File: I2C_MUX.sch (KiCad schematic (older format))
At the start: 25 parts, among them U5 TCA9548ARGER

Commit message: pcb progress
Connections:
- net labels removed: I2C_SFP3_SCL, I2C_SFP3_SDA, I2C_SFP4_SCL, I2C_SFP4_SDA
- wire segments 94 -> 90
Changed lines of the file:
@@
 Text HLabel 7850 3200 2    50   Output ~ 10
 I2C_SFP2_SCL
-Text HLabel 7850 3100 2    50   BiDi ~ 10
-I2C_SFP3_SDA
-Text HLabel 7850 3000 2    50   Output ~ 10
-I2C_SFP3_SCL
-Text HLabel 7850 2900 2    50   BiDi ~ 10
-I2C_SFP4_SDA
-Text HLabel 7850 2800 2    50   Output ~ 10
-I2C_SFP4_SCL
 Text HLabel 7850 2200 2    50   Output ~ 10
 I2C_FMC1_SCL
@@
 Text Label 7000 3300 0    50   ~ 10
 I2C_SFP2_SDA
-Text Label 7000 3000 0    50   ~ 10
-I2C_SFP3_SCL
-Text Label 7000 3100 0    50   ~ 10
-I2C_SFP3_SDA
-Text Label 7000 2800 0    50   ~ 10
-I2C_SFP4_SCL
-Text Label 7000 2900 0    50   ~ 10
-I2C_SFP4_SDA
 Text Label 7000 3400 0    50   ~ 10
 I2C_APP_SCL
@@
 	6000 3300 7850 3300
 Wire Wire Line
-	6000 3000 7850 3000
-Connection ~ 6000 3000
-Wire Wire Line
-	6000 3100 7850 3100
-Connection ~ 6000 3100
-Wire Wire Line
-	6000 2800 7850 2800
-Wire Wire Line
-	6000 2900 7850 2900
-Wire Wire Line
 	6000 3400 7850 3400
 Connection ~ 6000 3400
@@
 	6000 3700 7850 3700
 Connection ~ 6000 3700
-Connection ~ 6000 2800
-Connection ~ 6000 2900
 Connection ~ 6000 3200
 Connection ~ 6000 3300

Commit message: FPGA power finished, significant progress on PCB
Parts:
- U5: symbol AMC_FMC_Carrier-PcbDoc-rescue:TCA9548ARGER-Interface_Expansion-AMC_FMC_Carrier-PcbDoc-rescue -> AMC_FMC_Carrier-PcbDoc-rescue:TCA9548ARGER-Interface_Expansion-AMC_FMC_Carrier-PcbDoc-rescue-AMC_FMC_Carrier-PcbDoc-res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
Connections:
- net labels added: QSFP_SCL, QSFP_SDA
- net labels removed: I2C_SFP2_SCL, I2C_SFP2_SDA
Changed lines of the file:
@@
 $EndDescr
 $Comp
-L AMC_FMC_Carrier-PcbDoc-rescue:TCA9548ARGER-Interface_Expansion-AMC_FMC_Carrier-PcbDoc-rescue U5
+L AMC_FMC_Carrier-PcbDoc-rescue:TCA9548ARGER-Interface_Expansion-AMC_FMC_Carrier-PcbDoc-rescue-AMC_FMC_Carrier-PcbDoc-rescue-AMC_FMC_Carrier-PcbDoc-rescue U5
 U 1 1 5C5DB690
 P 5150 2900
@@
 I2C_SFP1_SCL
 Text HLabel 7850 3300 2    50   BiDi ~ 10
-I2C_SFP2_SDA
+QSFP_SDA
 Text HLabel 7850 3200 2    50   Output ~ 10
-I2C_SFP2_SCL
+QSFP_SCL
 Text HLabel 7850 2200 2    50   Output ~ 10
 I2C_FMC1_SCL
@@
 I2C_SFP1_SDA
 Text Label 7000 3200 0    50   ~ 10
-I2C_SFP2_SCL
+QSFP_SCL
 Text Label 7000 3300 0    50   ~ 10
-I2C_SFP2_SDA
+QSFP_SDA
 Text Label 7000 3400 0    50   ~ 10
 I2C_APP_SCL

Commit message: new board outline, rearranging banks connections, SODIMM memory
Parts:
- U5: symbol AMC_FMC_Carrier-PcbDoc-rescue:TCA9548ARGER-Interface_Expansion-AMC_FMC_Carrier-PcbDoc-rescue-AMC_FMC_Carrier-PcbDoc-rescue-AMC_FMC_Carrier-PcbDoc-rescue -> AMC_FMC_Carrier-PcbDoc-rescue:TCA9548ARGER-Interface_Expansion-AMC_FMC_Carrier-PcbDoc-rescue-AMC_FMC_Carrier-PcbDoc-rescue
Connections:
- net +3V3: no longer C40.2, R274.1, R39.1, R40.1, R41.1, U5.21 (VCC)
- net QSFP1_SCL: now reaches R53.1, U5.11 (SC4)
- net QSFP1_SDA: now reaches R54.1, U5.10 (SD4)
- net I2C_SFP1_SCL renamed I2C_CLK_SCL
- net I2C_SFP1_SDA renamed I2C_CLK_SDA
- net QSFP_SCL renamed QSFP2_SCL
- net QSFP_SDA renamed QSFP2_SDA
- new net +3.3VP: C40.2, R274.1, R39.1, R40.1, R41.1, U5.21 (VCC)
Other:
- note removed: "FMC1\n\n"
- note removed: "FMC2\n\n"
- note removed: "SFP1\n"
- note removed: "SFP2\n\n"
- note removed: "SFP3\n\n"
- note removed: "SFP4\n"
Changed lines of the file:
@@
 EESchema Schematic File Version 4
-LIBS:AMC_FMC_Carrier-PcbDoc-cache
 EELAYER 30 0
 EELAYER END
 $Descr A4 11693 8268
 encoding utf-8
-Sheet 7 25
+Sheet 5 25
 Title "Marble"
 Date "2019-01-16"
@@
 $EndDescr
 $Comp
-L AMC_FMC_Carrier-PcbDoc-rescue:TCA9548ARGER-Interface_Expansion-AMC_FMC_Carrier-PcbDoc-rescue-AMC_FMC_Carrier-PcbDoc-rescue-AMC_FMC_Carrier-PcbDoc-rescue U5
+L AMC_FMC_Carrier-PcbDoc-rescue:TCA9548ARGER-Interface_Expansion-AMC_FMC_Carrier-PcbDoc-rescue-AMC_FMC_Carrier-PcbDoc-rescue U5
 U 1 1 5C5DB690
 P 5150 2900
@@
 	1    0    0    -1
 $EndComp
-Text Notes 6600 2250 0    50   ~ 10
-FMC1\n\n
-Text Notes 6600 2450 0    50   ~ 10
-FMC2\n\n
-Text Notes 6600 2600 0    50   ~ 10
-SFP1\n
-Text Notes 6600 3250 0    50   ~ 10
-SFP2\n\n
-Text Notes 6600 3050 0    50   ~ 10
-SFP3\n\n
-Text Notes 6600 2800 0    50   ~ 10
-SFP4\n
-$Comp
-L power:+3V3 #PWR?
-U 1 1 5C5F9FA2
-P 5150 1700
-AR Path="/5BD32060/5C5F9FA2" Ref="#PWR?"  Part="1"
-AR Path="/5BABAC65/5C5F9FA2" Ref="#PWR?"  Part="1"
-AR Path="/5CC24E97/5C5F9FA2" Ref="#PWR?"  Part="1"
-AR Path="/5CC393D3/5C5F9FA2" Ref="#PWR?"  Part="1"
-AR Path="/5CC6DBF7/5C5F9FA2" Ref="#PWR?"  Part="1"
-AR Path="/5CC8AFE1/5C5F9FA2" Ref="#PWR?"  Part="1"
-AR Path="/5BCEDA3D/5C5F9FA2" Ref="#PWR065"  Part="1"
-F 0 "#PWR065" H 5150 1550 50  0001 C CNN
-F 1 "+3V3" H 5165 1873 50  0000 C CNN
-F 2 "" H 5150 1700 50  0001 C CNN
-F 3 "" H 5150 1700 50  0001 C CNN
-	1    5150 1700
-	1    0    0    -1
-$EndComp
 Wire Wire Line
 	5150 1700 5150 1800
@@
 Wire Wire Line
 	4600 3400 4750 3400
-Text HLabel 7850 2700 2    50   BiDi ~ 10
-I2C_SFP1_SDA
-Text HLabel 7850 2600 2    50   Output ~ 10
-I2C_SFP1_SCL
 Text HLabel 7850 3300 2    50   BiDi ~ 10
-QSFP_SDA
+QSFP2_SDA
 Text HLabel 7850 3200 2    50   Output ~ 10
-QSFP_SCL
+QSFP2_SCL
 Text HLabel 7850 2200 2    50   Output ~ 10
 I2C_FMC1_SCL
@@
 	6000 2450 6000 2500
 Wire Wire Line
-	6000 2550 6000 2600
-Wire Wire Line
-	6000 2650 6000 2700
-Wire Wire Line
 	6000 2750 6000 2800
 Wire Wire Line
 	6000 2850 6000 2900
 Wire Wire Line
-	6000 2950 6000 3000
-Wire Wire Line
-	6000 3050 6000 3100
-Wire Wire Line
 	6000 3150 6000 3200
 Wire Wire Line
@@
 	5550 2600 6000 2600
 Wire Wire Line
-	5550 2700 6000 2700
-Wire Wire Line
 	5550 2800 6000 2800
 Wire Wire Line
@@
 	1    0    0    -1
 $EndComp
-$Comp
-L power:+3V3 #PWR?
-U 1 1 5C2D28CD
-P 4050 1700
-AR Path="/5BD32060/5C2D28CD" Ref="#PWR?"  Part="1"
-AR Path="/5BABAC65/5C2D28CD" Ref="#PWR?"  Part="1"
-AR Path="/5CC24E97/5C2D28CD" Ref="#PWR?"  Part="1"
-AR Path="/5CC393D3/5C2D28CD" Ref="#PWR?"  Part="1"
-AR Path="/5CC6DBF7/5C2D28CD" Ref="#PWR?"  Part="1"
-AR Path="/5CC8AFE1/5C2D28CD" Ref="#PWR?"  Part="1"
-AR Path="/5BCEDA3D/5C2D28CD" Ref="#PWR062"  Part="1"
-F 0 "#PWR062" H 4050 1550 50  0001 C CNN
-F 1 "+3V3" H 4065 1873 50  0000 C CNN
-F 2 "" H 4050 1700 50  0001 C CNN
-F 3 "" H 4050 1700 50  0001 C CNN
-	1    4050 1700
-	1    0    0    -1
-$EndComp
 Wire Wire Line
 	4250 1750 4250 1700
@@
 Wire Wire Line
 	4050 1750 4050 1700
-Connection ~ 4050 1700
 Wire Wire Line
 	4050 2050 4050 2200
@@
 Text Label 7000 2500 0    50   ~ 10
 I2C_FMC2_SDA
-Text Label 7000 2600 0    50   ~ 10
-I2C_SFP1_SCL
-Text Label 7000 2700 0    50   ~ 10
-I2C_SFP1_SDA
 Text Label 7000 3200 0    50   ~ 10
-QSFP_SCL
+QSFP2_SCL
 Text Label 7000 3300 0    50   ~ 10
-QSFP_SDA
+QSFP2_SDA
 Text Label 7000 3400 0    50   ~ 10
 I2C_APP_SCL
@@
 Connection ~ 6000 2500
 Wire Wire Line
-	6000 2600 7850 2600
-Connection ~ 6000 2600
-Wire Wire Line
-	6000 2700 7850 2700
-Connection ~ 6000 2700
-Wire Wire Line
 	6000 3200 7850 3200
 Wire Wire Line
@@
 	0    1    1    0
 $EndComp
-$Comp
-L power:+3V3 #PWR?
-U 1 1 5D00ED85
-P 4450 2850
-AR Path="/5BD32060/5D00ED85" Ref="#PWR?"  Part="1"
-AR Path="/5BABAC65/5D00ED85" Ref="#PWR?"  Part="1"
-AR Path="/5CC24E97/5D00ED85" Ref="#PWR?"  Part="1"
-AR Path="/5CC393D3/5D00ED85" Ref="#PWR?"  Part="1"
-AR Path="/5CC6DBF7/5D00ED85" Ref="#PWR?"  Part="1"
-AR Path="/5CC8AFE1/5D00ED85" Ref="#PWR?"  Part="1"
-AR Path="/5BCEDA3D/5D00ED85" Ref="#PWR0648"  Part="1"
-F 0 "#PWR0648" H 4450 2700 50  0001 C CNN
-F 1 "+3V3" V 4450 3050 50  0000 C CNN
-F 2 "" H 4450 2850 50  0001 C CNN
-F 3 "" H 4450 2850 50  0001 C CNN
-	1    4450 2850
-	0    -1   -1   0
-$EndComp
 Wire Wire Line
 	4450 2850 4650 2850
@@
 Text Notes 2600 7300 0    79   ~ 16
 8 bit I2C addresses ( R/W bit = 0)
+Text HLabel 7850 3100 2    50   BiDi ~ 10
+QSFP1_SDA
+Text HLabel 7850 3000 2    50   Output ~ 10
+QSFP1_SCL
+Text Label 7000 3000 0    50   ~ 10
+QSFP1_SCL
+Text Label 7000 3100 0    50   ~ 10
+QSFP1_SDA
+Wire Wire Line
+	6000 3000 7850 3000
+Wire Wire Line
+	6000 3100 7850 3100
+Wire Wire Line
+	6000 2950 6000 3000
+Connection ~ 6000 3000
+Wire Wire Line
+	6000 3050 6000 3100
+Connection ~ 6000 3100
+Text HLabel 7850 2600 2    50   Output ~ 10
+I2C_CLK_SCL
+Text HLabel 7850 2700 2    50   BiDi ~ 10
+I2C_CLK_SDA
+Text Label 7000 2600 0    50   ~ 10
+I2C_CLK_SCL
+Text Label 7000 2700 0    50   ~ 10
+I2C_CLK_SDA
+Wire Wire Line
+	6000 2600 7850 2600
+Wire Wire Line
+	6000 2550 6000 2600
+Wire Wire Line
+	5550 2700 6000 2700
+Connection ~ 6000 2600
+Wire Wire Line
+	6000 2650 6000 2700
+Connection ~ 6000 2700
+Wire Wire Line
+	6000 2700 7850 2700
+$Comp
+L power:+3.3VP #PWR?
+U 1 1 5F60B33D
+P 5150 1700
+AR Path="/5C16C03C/5F60B33D" Ref="#PWR?"  Part="1"
+AR Path="/5BCEDA39/5F60B33D" Ref="#PWR?"  Part="1"
+AR Path="/5D05A99E/5F60B33D" Ref="#PWR?"  Part="1"
+AR Path="/5C16BF8E/5F60B33D" Ref="#PWR?"  Part="1"
+AR Path="/5F60B33D" Ref="#PWR?"  Part="1"
+AR Path="/5BCEDA3D/5F60B33D" Ref="#PWR?"  Part="1"
+F 0 "#PWR?" H 5150 1550 50  0001 C CNN
+F 1 "+3V3MP" H 5165 1873 50  0000 C CNN
+F 2 "" H 5150 1700 50  0001 C CNN
+F 3 "" H 5150 1700 50  0001 C CNN
+	1    5150 1700
+	1    0    0    -1
+$EndComp
+$Comp
+L power:+3.3VP #PWR?
+U 1 1 5F60D5A3
+P 4050 1700
+AR Path="/5C16C03C/5F60D5A3" Ref="#PWR?"  Part="1"
+AR Path="/5BCEDA39/5F60D5A3" Ref="#PWR?"  Part="1"
+AR Path="/5D05A99E/5F60D5A3" Ref="#PWR?"  Part="1"
+AR Path="/5C16BF8E/5F60D5A3" Ref="#PWR?"  Part="1"
+AR Path="/5F60D5A3" Ref="#PWR?"  Part="1"
+AR Path="/5BCEDA3D/5F60D5A3" Ref="#PWR?"  Part="1"
+F 0 "#PWR?" H 4050 1550 50  0001 C CNN
+F 1 "+3V3MP" H 4065 1873 50  0000 C CNN
+F 2 "" H 4050 1700 50  0001 C CNN
+F 3 "" H 4050 1700 50  0001 C CNN
+	1    4050 1700
+	1    0    0    -1
+$EndComp
+$Comp
+L power:+3.3VP #PWR?
+U 1 1 5F60F78D
+P 4450 2850
+AR Path="/5C16C03C/5F60F78D" Ref="#PWR?"  Part="1"
+AR Path="/5BCEDA39/5F60F78D" Ref="#PWR?"  Part="1"
+AR Path="/5D05A99E/5F60F78D" Ref="#PWR?"  Part="1"
+AR Path="/5C16BF8E/5F60F78D" Ref="#PWR?"  Part="1"
+AR Path="/5F60F78D" Ref="#PWR?"  Part="1"
+AR Path="/5BCEDA3D/5F60F78D" Ref="#PWR?"  Part="1"
+F 0 "#PWR?" H 4450 2700 50  0001 C CNN
+F 1 "+3V3MP" V 4450 3100 50  0000 C CNN
+F 2 "" H 4450 2850 50  0001 C CNN
+F 3 "" H 4450 2850 50  0001 C CNN
+	1    4450 2850
+	0    -1   -1   0
+$EndComp
+Connection ~ 4050 1700
 $EndSCHEMATC

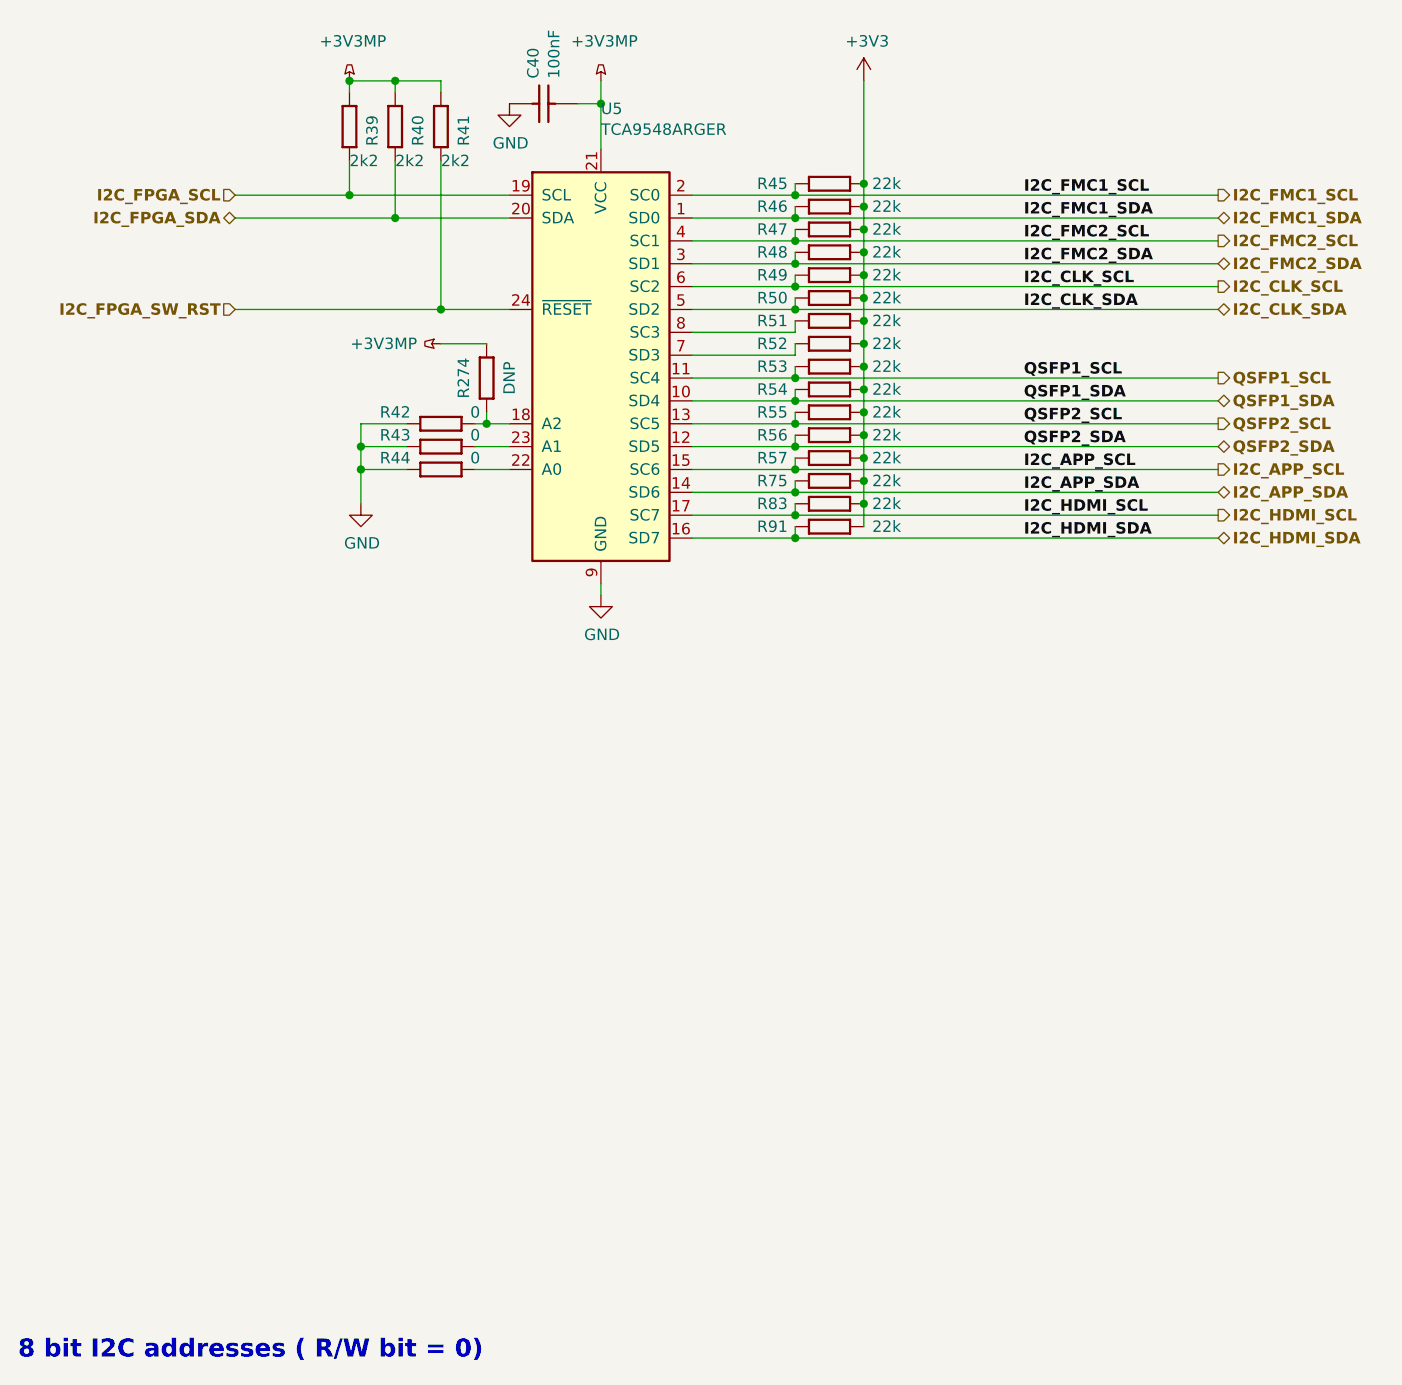
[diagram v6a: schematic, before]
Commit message: DDR lenght mached, 2 additional LEDs added, I2C pullups voltage changed and other minor changes
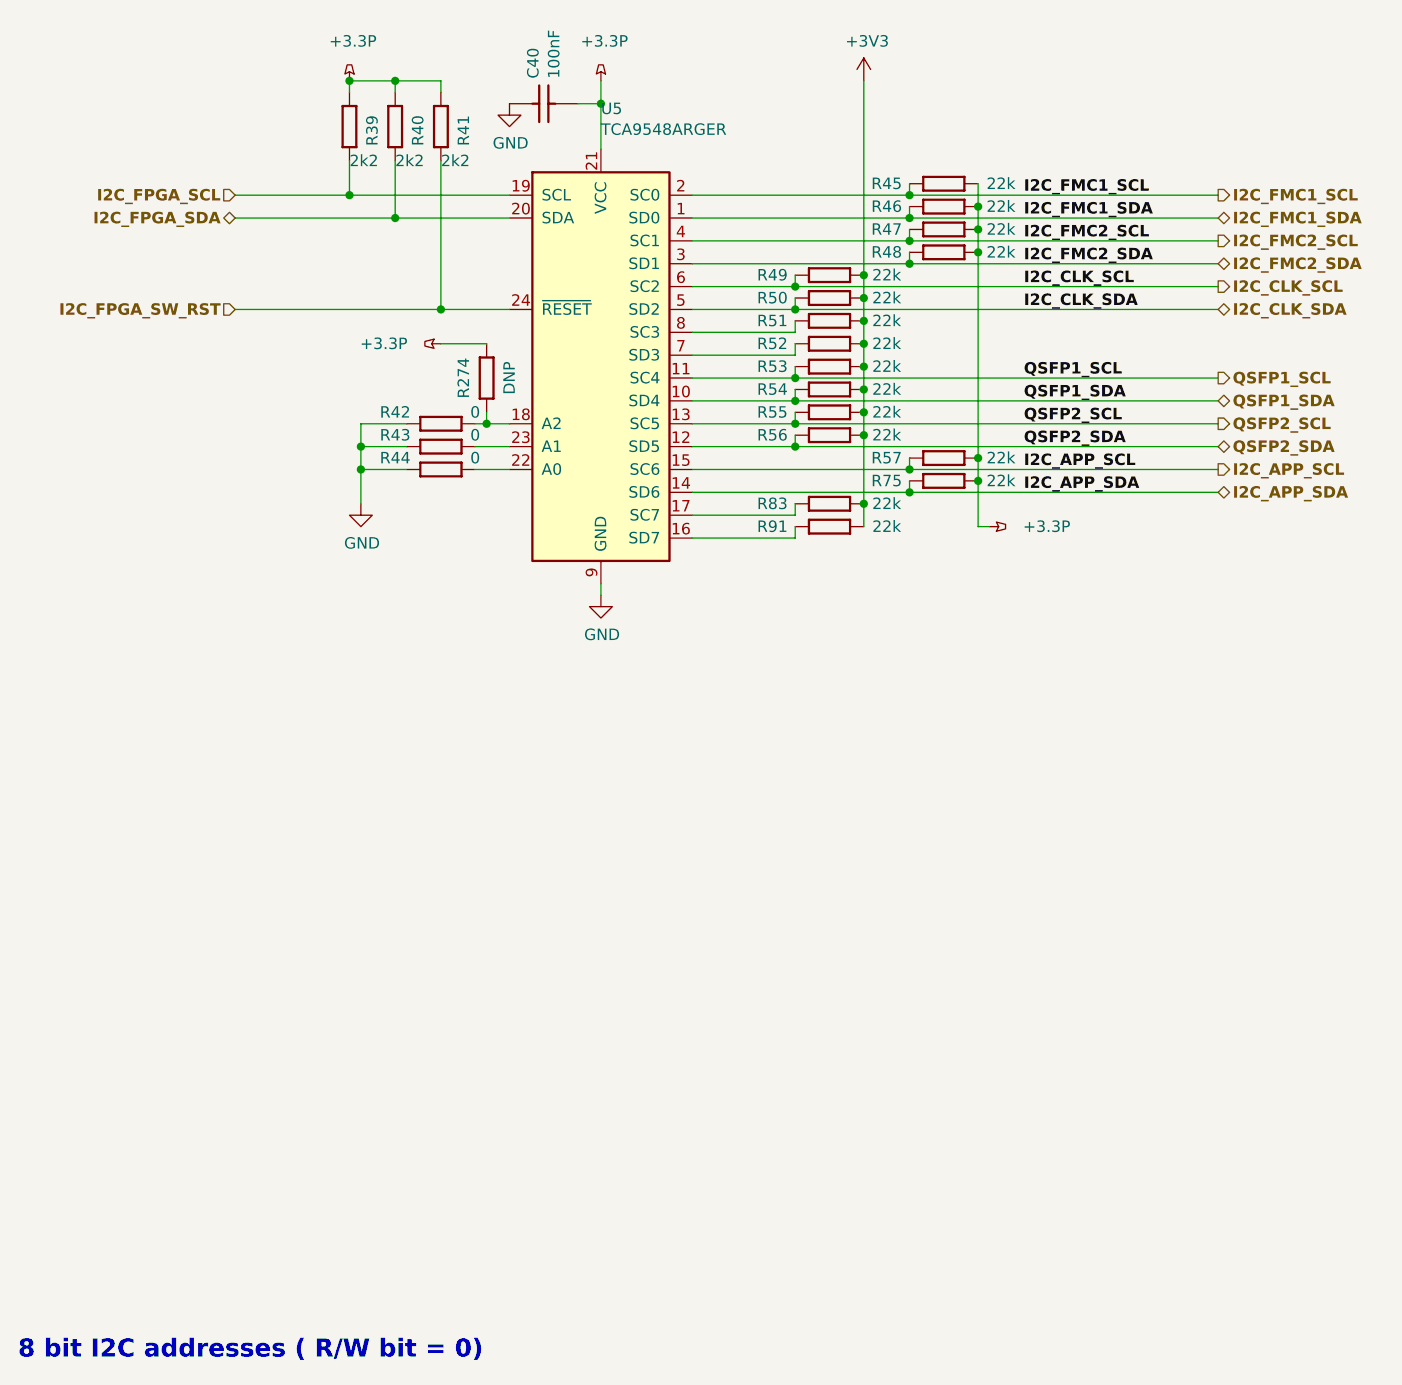
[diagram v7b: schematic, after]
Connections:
- net +3V3: no longer R45.2, R46.2, R47.2, R48.2, R57.2, R75.2
- net +3.3VP renamed +3.3P
- net +3.3P: now also R45.2, R46.2, R47.2, R48.2, R57.2, R75.2
- net I2C_HDMI_SCL: no longer names the net of R83.1, U5.17 (SC7)
- net I2C_HDMI_SDA: no longer names the net of R91.1, U5.16 (SD7)
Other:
- moved on the sheet: R45, R46, R47, R48, R57, R75

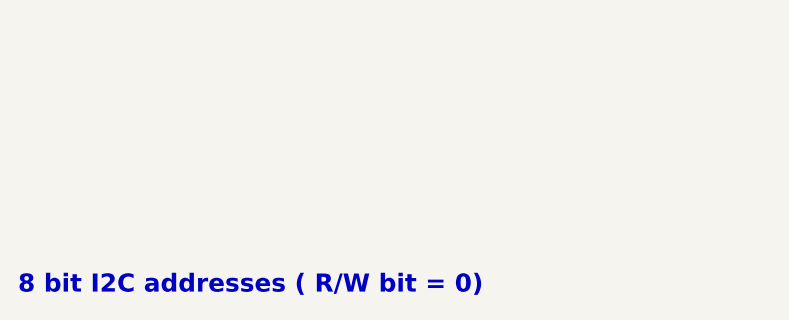
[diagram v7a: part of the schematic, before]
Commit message: new I2C diagram, CLK_RST -> IO expander
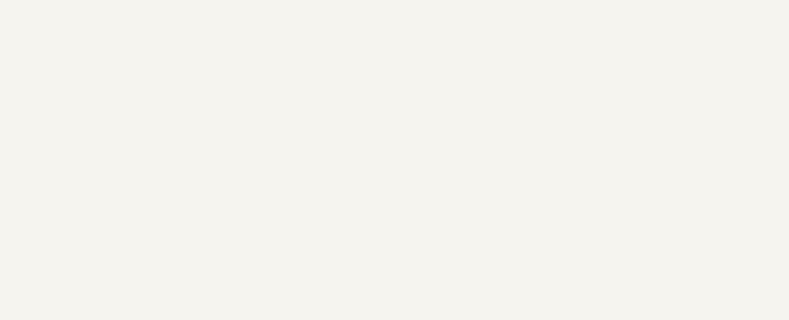
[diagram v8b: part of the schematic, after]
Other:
- note removed: "8 bit I2C addresses ( R/W bit = 0)"
